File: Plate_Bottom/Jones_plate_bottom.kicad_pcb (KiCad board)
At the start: 2 copper layers, 285 x 94.6 mm, 11 parts

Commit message: v04発注
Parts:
- removed H1, H10, H2, H3, H4, H5, H6, H7, H8, H9: MountingHole, MountingHole:MountingHole_2.2mm_M2
- removed the REF** at (157.9, 64.4)
- added H20: MountingHole, MountingHole:MountingHole_2.2mm_M2, F.Cu at (110.8, 19.8)
- added H21: MountingHole, MountingHole:MountingHole_2.2mm_M2, F.Cu at (205.9, 19.8)
- added H22: MountingHole, MountingHole:MountingHole_2.2mm_M2, F.Cu at (99.3, 108.9)
- added H23: MountingHole, MountingHole:MountingHole_2.2mm_M2, F.Cu at (190.7, 108.9)
- added REF**: 60_Outline, locallib:60_Outline_for_Bottom_USB_cutout_slit_closed, F.Cu at (157.9, 64.4)
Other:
- outline, holes or cut-outs redrawn
- board text added: "#Jones Bottom Plate v.0.4.1 @jpskenn"
- board text added: "USB connector"
- board text removed: "#Jones Bottom Plate v.0.4 @jpskenn"

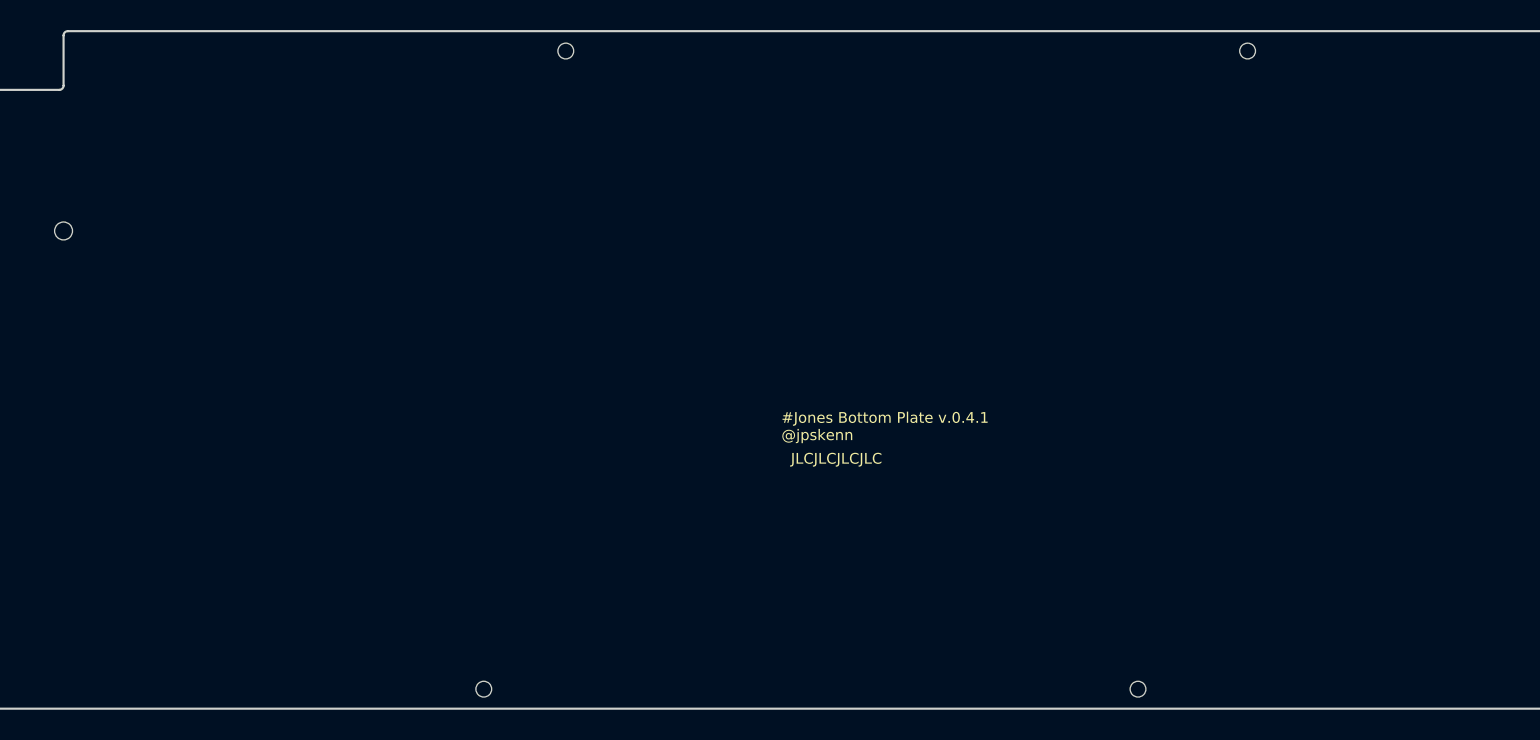
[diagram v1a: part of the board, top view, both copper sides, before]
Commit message: ボトムプレート：ネジ位置、RSW窓開け、ロゴ、Ver.表記
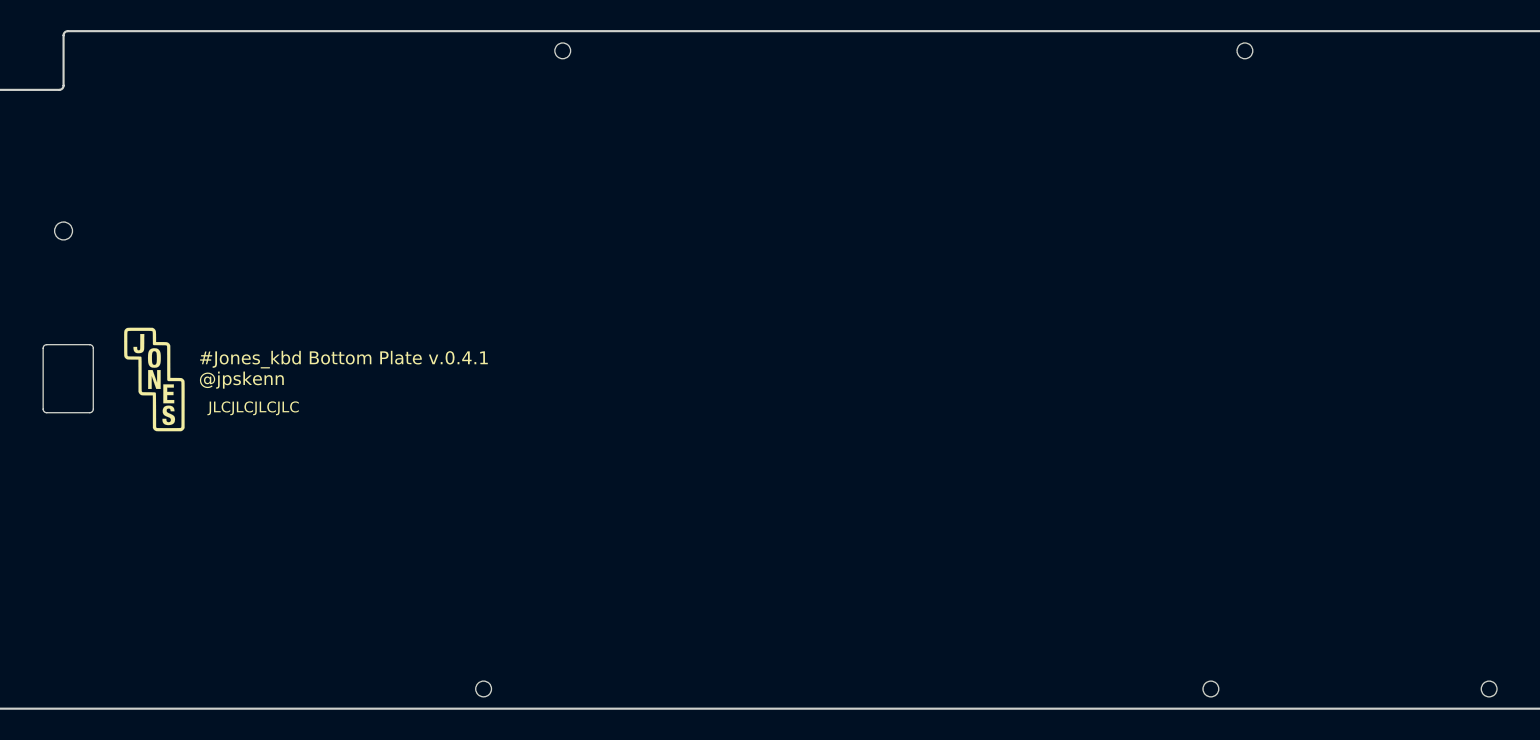
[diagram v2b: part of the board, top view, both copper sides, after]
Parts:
- removed H20, H21, H22, H23: MountingHole, MountingHole:MountingHole_2.2mm_M2
- added G***: LOGO, locallib:Jones_logo_8.8x15, F.Cu at (53.3, 65.8)
- added H1: MountingHole, MountingHole:MountingHole_2.2mm_M2, F.Cu at (110.3, 19.8)
- added H2: MountingHole, MountingHole:MountingHole_2.2mm_M2, F.Cu at (205.6, 19.8)
- added H3: MountingHole, MountingHole:MountingHole_2.2mm_M2, F.Cu at (99.3, 108.9)
- added H4: MountingHole, MountingHole:MountingHole_2.2mm_M2, F.Cu at (200.8, 108.9)
- added H5: MountingHole, MountingHole:MountingHole_2.2mm_M2, F.Cu at (239.7, 108.9)
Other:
- board text added: "#Jones_kbd Bottom Plate v.0.4.1 @jpskenn"
- board text removed: "#Jones Bottom Plate v.0.4.1 @jpskenn"

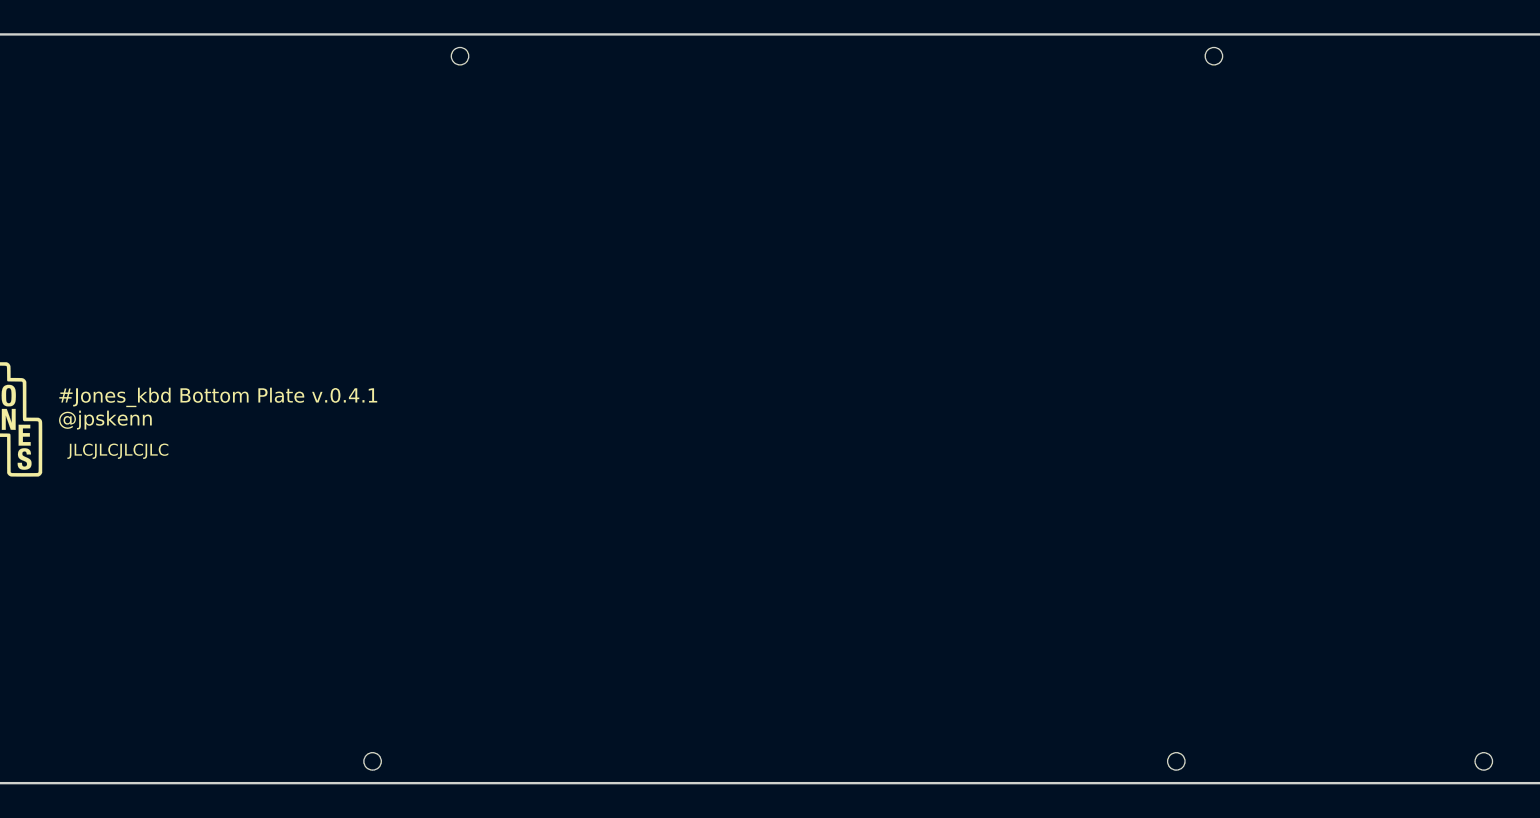
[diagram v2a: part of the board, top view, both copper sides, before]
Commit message: 基板とボトムをつなぐネジ位置の変更を反映
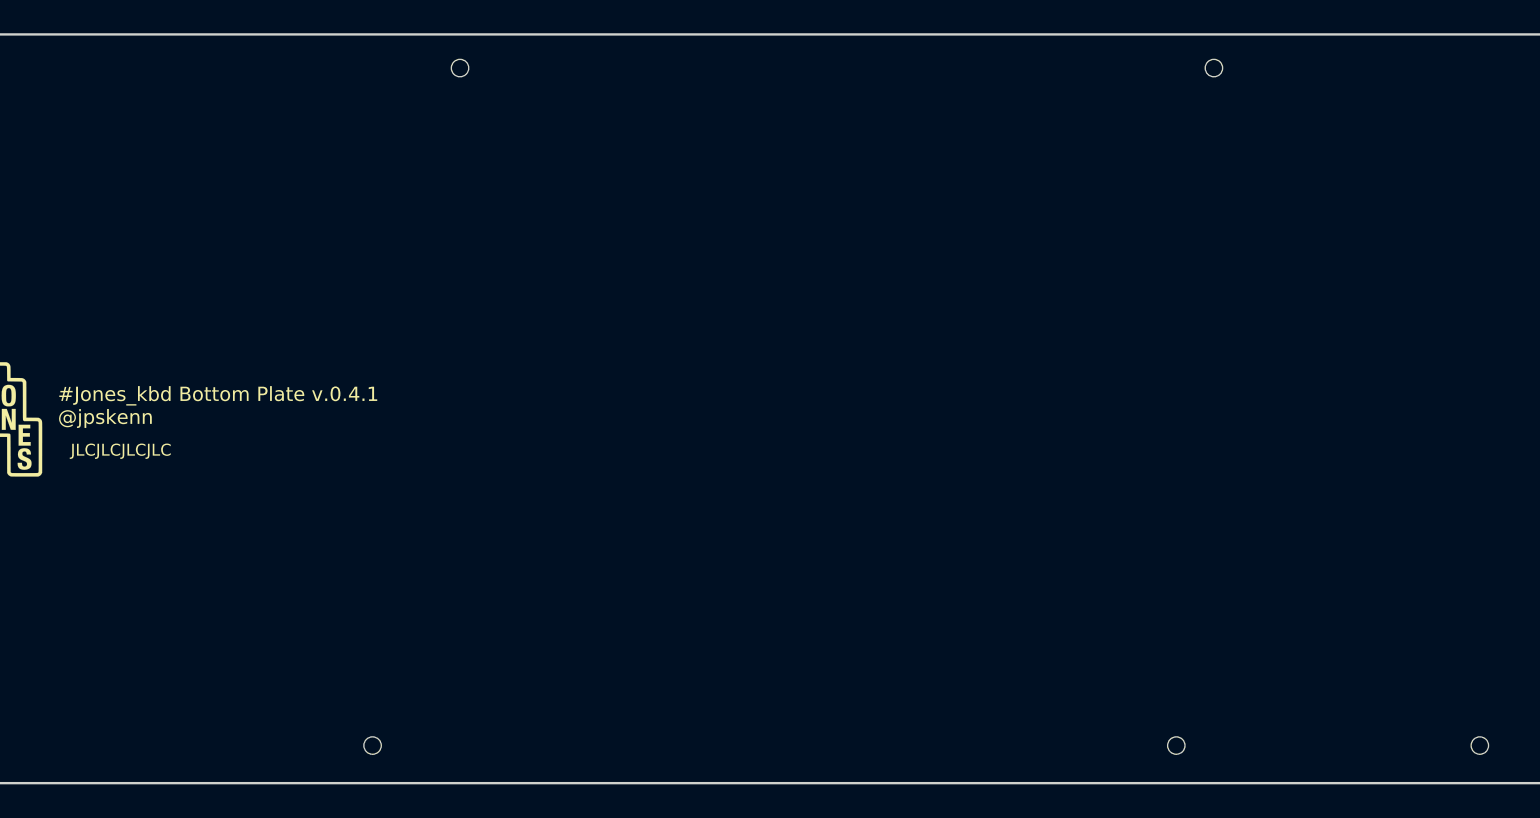
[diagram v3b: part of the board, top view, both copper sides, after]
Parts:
- moved H5 2.06 mm to (239.2, 106.9)
- moved H3 2.00 mm to (99.3, 106.9)
- moved H4 2.00 mm to (200.8, 106.9)
- moved H1 1.50 mm to (110.3, 21.3)
- moved H2 1.50 mm to (205.6, 21.3)

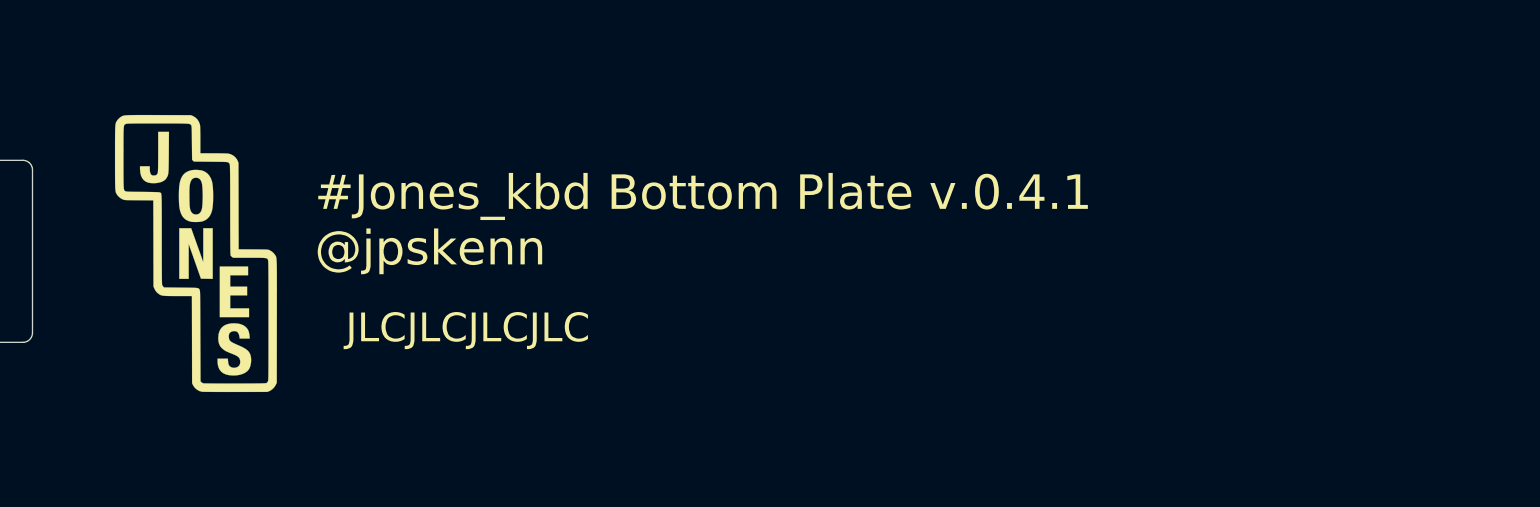
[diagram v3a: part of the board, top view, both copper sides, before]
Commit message: ゴム足ガイド変更。ロゴ、バージョン更新。
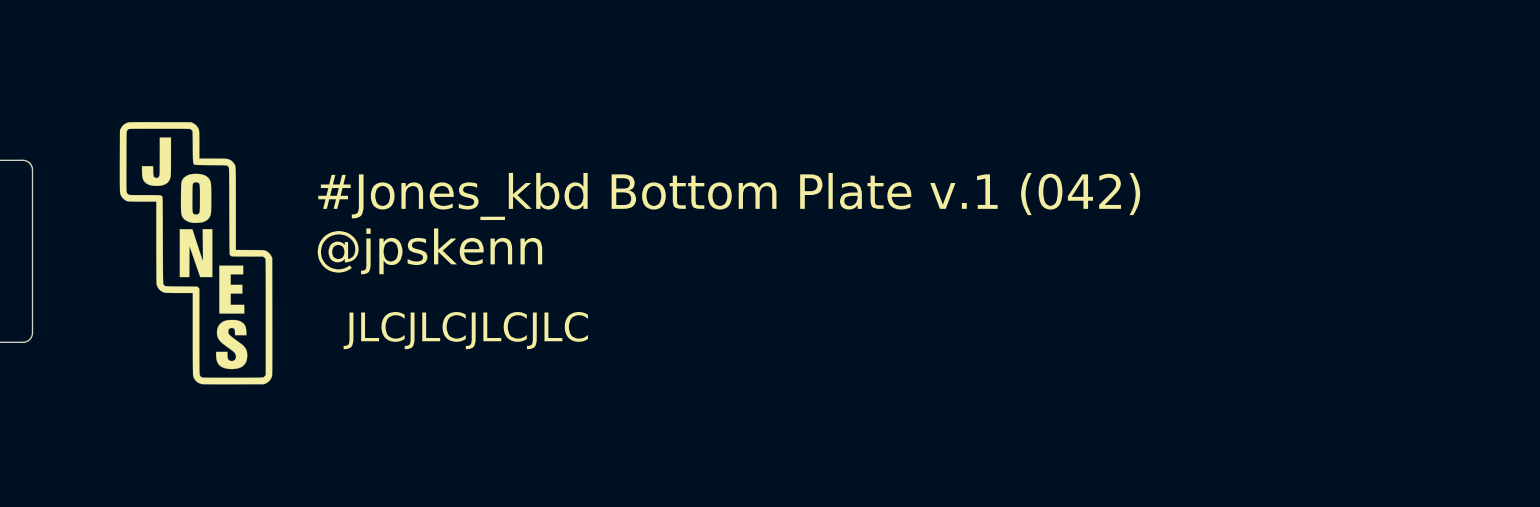
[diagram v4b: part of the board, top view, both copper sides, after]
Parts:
- removed the G*** at (53.3, 65.8)
- added G***: LOGO, locallib:Jones_logo_B_8.3x13.9, F.Cu at (53.3, 65.7)
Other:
- board text added: "#Jones_kbd Bottom Plate v.1 (042) @jpskenn"
- board text removed: "#Jones_kbd Bottom Plate v.0.4.1 @jpskenn"
